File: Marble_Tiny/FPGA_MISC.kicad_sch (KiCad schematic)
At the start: 20 parts, among them T3 BSS138LT1G, U1 XC7A35T-CSG325, U27 S25FL128SAGMFI001, U9 REF3012

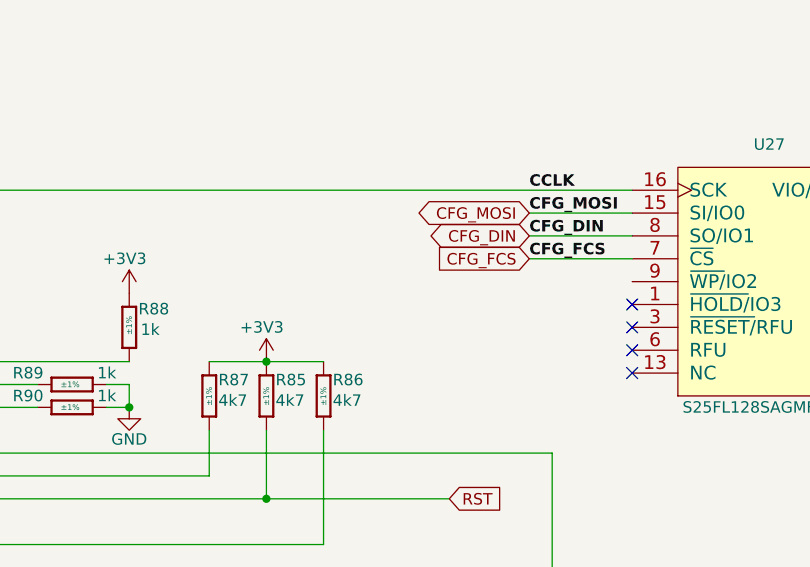
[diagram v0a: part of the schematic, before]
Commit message: fixed ERCs; added test points; added WP switch
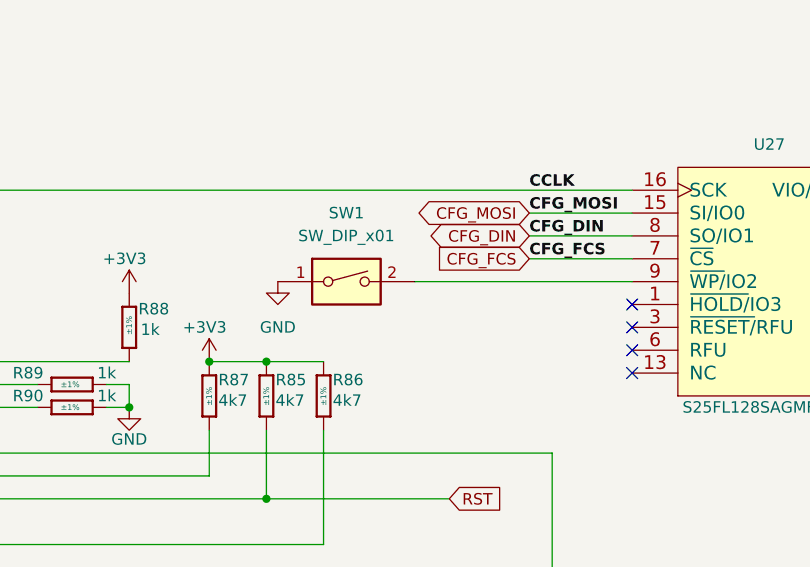
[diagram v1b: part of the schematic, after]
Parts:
- added SW1: SW_DIP_x01, Switches:SW_OMRON_A6SN-1101, symbol Switch:SW_DIP_x01
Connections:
- net GND: now also SW1.1
- net at U27.9 (~{WP/}IO2): now also SW1.2
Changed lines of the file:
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@@
 	)
 	(junction
+		(at 168.91 83.82)
+		(diameter 0)
+		(color 0 0 0 0)
+	)
+	(junction
 		(at 246.38 64.77)
 		(diameter 0)
@@
 	(wire
 		(pts
+			(xy 191.77 74.93) (xy 215.9 74.93)
+		)
+		(stroke
+			(width 0)
+			(type default)
+		)
+	)
+	(wire
+		(pts
 			(xy 175.26 99.06) (xy 175.26 91.44)
 		)
@@
 	)
 	(symbol
+		(lib_id "Switch:SW_DIP_x01")
+		(at 184.15 74.93 0)
+		(unit 1)
+		(exclude_from_sim no)
+		(in_bom yes)
+		(on_board yes)
+		(dnp no)
+		(fields_autoplaced yes)
+		(property "Reference" "SW1"
+			(at 184.15 67.31 0)
+			(effects
+				(font
+					(size 1.27 1.27)
+				)
+			)
+		)
+		(property "Value" "SW_DIP_x01"
+			(at 184.15 69.85 0)
+			(effects
+				(font
+					(size 1.27 1.27)
+				)
+			)
+		)
+		(property "Footprint" "Switches:SW_OMRON_A6SN-1101"
+			(at 184.15 74.93 0)
+			(effects
+				(font
+					(size 1.27 1.27)
+				)
+				(hide yes)
+			)
+		)
+		(property "Datasheet" "~"
+			(at 184.15 74.93 0)
+			(effects
+				(font
+					(size 1.27 1.27)
+				)
+				(hide yes)
+			)
+		)
+		(property "Description" "1x DIP Switch, Single Pole Single Throw (SPST) switch, small symbol"
+			(at 184.15 74.93 0)
+			(effects
+				(font
+					(size 1.27 1.27)
+				)
+				(hide yes)
+			)
+		)
+		(pin "2"
+		)
+		(pin "1"
+		)
+		(instances
+			(project ""
+				(path "/c2a4f786-b14c-434a-acf7-b20fb2221b0b/74b17685-a06b-496e-ad9c-4554e740129f"
+					(reference "SW1")
+					(unit 1)
+				)
+			)
+		)
+	)
+	(symbol
 		(lib_id "power:GND")
 		(at 160.02 138.43 0)
@@
 	(symbol
 		(lib_id "power:+1V0")
-		(at 175.26 83.82 0)
+		(at 168.91 83.82 0)
 		(unit 1)
 		(exclude_from_sim no)
@@
 		(dnp no)
 		(property "Reference" "#PWR0129"
-			(at 175.26 87.63 0)
+			(at 168.91 87.63 0)
 			(effects
 				(font
@@
 		)
 		(property "Value" "+3V3"
-			(at 174.752 80.01 0)
+			(at 168.402 80.01 0)
 			(effects
 				(font
@@
 		)
 		(property "Footprint" ""
-			(at 175.26 83.82 0)
+			(at 168.91 83.82 0)
 			(effects
 				(font
@@
 		)
 		(property "Datasheet" ""
-			(at 175.26 83.82 0)
+			(at 168.91 83.82 0)
 			(effects
 				(font
@@
 		)
 		(property "Description" "Power symbol creates a global label with name \"+1V0\""
-			(at 175.26 83.82 0)
+			(at 168.91 83.82 0)
 			(effects
 				(font
@@
 					(unit 1)
 				)
+			)
+		)
+	)
+	(symbol
+		(lib_id "power:GND")
+		(at 176.53 74.93 0)
+		(unit 1)
+		(exclude_from_sim no)
+		(in_bom yes)
+		(on_board yes)
+		(dnp no)
+		(fields_autoplaced yes)
+		(property "Reference" "#PWR0343"
+			(at 176.53 81.28 0)
+			(effects
+				(font
+					(size 1.27 1.27)
+				)
+				(hide yes)
+			)
+		)
+		(property "Value" "GND"
+			(at 176.53 80.01 0)
+			(effects
+				(font
+					(size 1.27 1.27)
+				)
+			)
+		)
+		(property "Footprint" ""
+			(at 176.53 74.93 0)
+			(effects
+				(font
+					(size 1.27 1.27)
+				)
+				(hide yes)
+			)
+		)
+		(property "Datasheet" ""
+			(at 176.53 74.93 0)
+			(effects
+				(font
+					(size 1.27 1.27)
+				)
+				(hide yes)
+			)
+		)
+		(property "Description" "Power symbol creates a global label with name \"GND\" , ground"
+			(at 176.53 74.93 0)
+			(effects
+				(font
+					(size 1.27 1.27)
+				)
+				(hide yes)
+			)
+		)
+		(pin "1"
+		)
+		(instances
+			(project "Marble_Tiny"
+				(path "/c2a4f786-b14c-434a-acf7-b20fb2221b0b/74b17685-a06b-496e-ad9c-4554e740129f"
+					(reference "#PWR0343")
+					(unit 1)
+				)

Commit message: fixed issue with PMODs; added board name and revision; fixed polygons issue
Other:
- company: (none) -> ${name}
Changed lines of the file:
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@@
 	(generator_version "9.0")
 	(paper "A4")
+	(title_block
+		(date "2025-04-18")
+		(rev "${rev}")
+		(company "${name}")
+		(comment 1 "${author}")
+	)
 	(text "FPGA DONE"
 		(exclude_from_sim no)
